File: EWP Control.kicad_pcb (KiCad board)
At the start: 2 copper layers, 170 x 130 mm, 93 parts, among them Q1 SQJ411EP-T1_GE3, SW1 HX 3X4X2.5-PA-4N PUSH BUTTON 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, U1 RP2350B_C42415655, U10 BME280, U11 DS3231MZ+, U12 INA226AIDGSR, U13 TPL5010DDCR, U14 BTS50015-1TAD, U15 BTS50015-1TAD, U2 ESP32-S3, U3 W25Q128JVSIQTR, U4 MT25QL01GBBB8ESF-0SIT TR, U5 APS51208N-OBR-BD, U6 AD7124-8BCPZ, U7 AD5689RBRUZ, U8 TPS54540DDAR, U9 TLV75533PDBVR, X1 X49SM12MSD2SI, X2 X49SM12MSD2SI, X3 HSO531S 12MHZ 1.6~3.6V, X4 40MHZ/3225/12PF/10PPM

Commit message: Complete schematic circuit design + 4-layer PCB structure/zones/basic routing
Schematic (EWP Control.kicad_sch):
- Full netlist design for all 16 ICs + 55 caps + 32 resistors + crystals/
  inductors/diodes/MOSFET/switch/connectors via tools/fix_schematic.py
- 527 local labels define 96 nets; 106 no_connects for unused pins;
  13 PWR_FLAG symbols drive all power nets (ERC pin_not_connected=0,
  power_pin_not_driven=0)
- 0 floating pins across all 697 component pins (was 697 floating)
- Each pin->net traceable to factory_config.h (ESP32-S3) or P01-P15 page
  plan (RP2350B/ADC/DAC/power/sensors/actuators)
- GPIO48 (absent on ESP32-S3 QFN-56) -> RGB moved to GPIO38 (pin 43)

PCB (EWP Control.kicad_pcb):
- 4-layer stack: F.Cu / In1.Cu(GND) / In2.Cu(PWR) / B.Cu (was 2-layer)
- Board outline compacted 170x130 -> 78x66 mm
- 4 copper zones: GND full-board on In1.Cu; +3.3V/+5V/VBAT on In2.Cu
- 216 trace items: 137 segments (SPI/I2C/UART/QSPI buses) + 79 power vias
  tying every IC power pad to inner planes
- Pad netlist re-annotated from fresh schematic (92 nets on pads)

Firmware:
- SC_FACTORY_PIN_RGB 48 -> 38 (matches QFN-56 pin 43)
- verify_release.py: release_static_gate = ok
- verify_control_math.py: 94.7% steady quality
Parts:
- moved C36 354.7 mm to (70.0, 56.0)
- moved C29 351.5 mm to (70.0, 49.5)
- moved C3 348.7 mm to (70.0, 43.0)
- moved C39 346.1 mm to (70.0, 36.5)
- moved C13 343.9 mm to (70.0, 30.0)
- moved R10 342.0 mm to (70.0, 23.5)
- moved R5 340.4 mm to (70.0, 17.0)
- moved U15 339.7 mm to (70.0, 4.00)
- moved U6 339.2 mm to (70.0, 10.5)
- moved C33 339.0 mm to (65.0, 56.0)
- moved C44 335.7 mm to (65.0, 49.5)
- moved C2 332.7 mm to (65.0, 43.0)
- moved C35 330.0 mm to (65.0, 36.5)
- moved R14 327.7 mm to (65.0, 30.0)
- moved C45 325.8 mm to (57.5, 56.0)
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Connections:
- net DAC_OUTA renamed DAC_VOUTA
- net DAC_OUTB renamed DAC_VOUTB
- net N_01AE718B renamed RF_ANT
- net N_07AE7AFD renamed PUMP_SSR
- net N_2B5D0ED9 renamed VBAT_SENSE
- net N_345D1D04 renamed V5V_SENSE
- net N_355D1E97 renamed PUMP_VSENSE
- net N_45931B8A renamed GPIO47_ADC7
- net N_4927DEA4 renamed RTC_RST
- net N_589CFCC9 renamed SD_MISO
- net N_5F9D07CE renamed ECU_REQUEST
- net N_609D0961 renamed FAN_SSR
- net N_639D0E1A renamed SD_MOSI
- net N_9C85E4E0 renamed VREF_OUT
- net N_F8AE6360 renamed PUMP_PWM
- net N_F9AE64F3 renamed FAN_PWM
- net PWR_OUT2 renamed FAN_OUT
- net PWR_SW_CTRL renamed PUMP_GATE
- net SHUNT_N renamed ISENSE_NEG
- net USB_D_N renamed RP_USB_DM
- net USB_D_P renamed RP_USB_DP
- C1 pad 1: +3.3V -> (no net)
- C1 pad 2: GND -> (no net)
- C10 pad 1: +3.3V -> VBAT
- C11 pad 1: GND -> VBAT
- C11 pad 2: +3.3V -> GND
- C12 pad 1: REGCAPA -> GND
- C13 pad 1: REGCAPD -> GND
- C14 pad 1: +3.3V -> GND
- C15 pad 1: +3.3V -> GND
- C18 pad 1: +3.3V -> GND
- C19 pad 1: +3.3V -> GND
- C2 pad 1: +3.3V -> GND
- C21 pad 1: VREF -> +3.3V
- C22 pad 1: +3.3V -> GND
- C23 pad 1: +3.3V -> VBAT
- C24 pad 1: VIN -> +5V
- C25 pad 1: N_U8_BOOT -> +5V
- C25 pad 2: VSW -> GND
- C26 pad 1: N_B85409EF -> +5V
- C27 pad 1: N_U8_COMP -> BUCK_COMP
- C27 pad 2: N_U8_COMP_S -> GND
- C28 pad 1: N_U8_COMP -> BUCK_FB
- C29 pad 1: +3.3V -> GND
- C3 pad 1: +3.3V -> GND
- C32 pad 1: VSYS -> GND
- C34 pad 2: +3.3V -> GND
- C35 pad 1: N_0EF52E9F -> +3.3V
- C35 pad 2: N_0FF53032 -> GND
- C37 pad 1: +3.3V -> VBAT
- C39 pad 1: N_BA54E6B3 -> GND
- C39 pad 2: N_BB54E846 -> GND
- C4 pad 1: +3.3V -> GND
- C41 pad 1: N_1D9BD64C -> GND
- C41 pad 2: N_209BDB05 -> GND
- C42 pad 1: +3.3V -> GND
- C44 pad 1: +3.3V -> GND
- C45 pad 2: +3.3V -> GND
- C5 pad 1: +3.3V -> GND
- C6 pad 1: +3.3V -> DVDD
- C7 pad 1: 1v1 -> GND
- Card1 pad 11: N_AC34DDE2 -> GND
- Card1 pad 12: N_AB34DC4F -> GND
- Card1 pad 2: HS_SW2_EN -> SD_CS
- Card1 pad 5: MCU_WDT_WAKE -> SD_SCK
- Card1 pad 8: MCU_WDT_DONE -> SD_DAT1
- Card1 pad SW2: +3.3V -> GND
- D1 pad 1: ESP_GPIO0_BOOT -> VBAT
- D1 pad 2: N_8DADAF7E -> +5V
- L1 pad 2: 1v1 -> DVDD
- L2 pad 1: VREG_LX -> (no net)
- L2 pad 2: 1v1 -> (no net)
- Q1 pad 1: VSYS -> GND
- Q1 pad 2: VSYS -> PUMP_CTRL
- Q1 pad 3: VSYS -> PUMP_CTRL
- Q1 pad 5: VIN -> PUMP_OUT
- R1 pad 1: PSRAM_DQ6 -> MCU_STATUS_LED
- R10 pad 1: HS_SW1_IS -> +3.3V
- R11 pad 1: HS_SW2_IS -> PUMP_ISENSE
- R12 pad 1: WDT_DELAY -> WATCHDOG_WAKE
- R12 pad 2: GND -> +3.3V
- R13 pad 2: VIN -> GND
- R14 pad 1: vsys -> RP_RUN
- R14 pad 2: N_85E97F04 -> +3.3V
- R15 pad 1: HS_SW1_IS -> RGB_DIN
- R15 pad 2: GND -> RGB_LED
- R16 pad 1: +3.3V -> FAN_ISENSE
- R16 pad 2: INA_ALERT -> GND
- R17 pad 1: WDT_DELAY -> ESP_RESET
- R18 pad 1: +3.3V -> USB_CC1
- R18 pad 2: PSRAM_CE -> GND
- R19 pad 1: INA_ALERT -> USB_CC2
- R19 pad 2: +3.3V -> GND
- R2 pad 1: +3.3V -> ESP_BOOT
- R2 pad 2: ESP_CHIP_PU_EN -> +3.3V
- R20 pad 2: BME_CSB -> NTC_COOLANT
- R22 pad 1: HS_SW1_EN -> ISENSE_POS
- R22 pad 2: GND -> +3.3V
- R23 pad 1: HS_SW2_IS -> SD_CD
- R23 pad 2: GND -> +3.3V
- R3 pad 1: SD_CD -> ESP_RESET
- R4 pad 1: N_CBA97650 -> VBAT
- R4 pad 2: VIN -> GND
- R5 pad 1: N_A35168C1 -> BUCK_FB
- R5 pad 2: N_U8_FB -> GND
- R6 pad 1: N_U8_FB -> +5V
- R6 pad 2: GND -> BUCK_FB
- R7 pad 1: N_U8_RT -> BUCK_COMP
- R7 pad 2: GND -> BUCK_FB
- R8 pad 1: N_U8_COMP_S -> +3.3V
- R9 pad 1: BME_CSB -> I2C_SDA
- SW1 pad 1: ESP_CHIP_PU_EN -> GND
- SW1 pad 2: ESP_CHIP_PU_EN -> ESP_RESET
- SW1 pad 4: GND -> ESP_RESET
- U1 pad 1: N_917A5B02 -> (no net)
- U1 pad 10: 1v1 -> DVDD
- U1 pad 11: QSPI1_IO3 -> ADC_MISO
- U1 pad 12: QSPI1_SCLK -> ADC_CS
- U1 pad 13: QSPI1_CS -> DAC_CS
- U1 pad 14: N_399D9602 -> (no net)
- U1 pad 16: SD_DAT0 -> PUMP_CTRL
- U1 pad 17: MCU_WDT_DONE -> FAN_CTRL
- U1 pad 18: MCU_WDT_WAKE -> MCU_UART_TX
- U1 pad 19: SD_CMD -> MCU_UART_RX
- U1 pad 2: N_907A596F -> (no net)
- U1 pad 20: SD_DAT2 -> MCU_HEARTBEAT
- U1 pad 21: HS_SW2_EN -> ESP_RESET
- U1 pad 22: SD_CD -> MCU_STATUS_LED
- U1 pad 23: N_CC9AABD4 -> WATCHDOG_FEED
- U1 pad 25: N_CA9AA8AE -> (no net)
- U1 pad 26: N_C99AA71B -> (no net)
- U1 pad 27: N_C89AA588 -> (no net)
- U1 pad 28: N_C79AA3F5 -> (no net)
- U1 pad 3: N_8F7A57DC -> (no net)
- U1 pad 32: 1v1 -> DVDD
- U1 pad 34: PSRAM_DQ7 -> RP_SWDIO
- U1 pad 35: PSRAM_DQ6 -> RP_RUN
- U1 pad 36: PSRAM_DQ5 -> (no net)
- U1 pad 37: PSRAM_DQ4 -> (no net)
- U1 pad 38: PSRAM_DQ3 -> (no net)
- U1 pad 39: PSRAM_DQ2 -> (no net)
- U1 pad 4: N_8E7A5649 -> (no net)
- U1 pad 40: PSRAM_DQ1 -> (no net)
- U1 pad 42: PSRAM_DQ0 -> (no net)
- U1 pad 43: PSRAM_CLK -> (no net)
- U1 pad 44: PSRAM_CE -> (no net)
- U1 pad 45: PSRAM_DQS -> (no net)
- U1 pad 46: PSRAM_RST -> (no net)
- U1 pad 47: N_C896285A -> (no net)
- U1 pad 48: N_BB9613E3 -> (no net)
- U1 pad 49: N_BA961250 -> (no net)
- U1 pad 51: 1v1 -> DVDD
- U1 pad 52: N_3B930BCC -> (no net)
- U1 pad 53: N_3C930D5F -> (no net)
- U1 pad 54: N_399308A6 -> (no net)
- U1 pad 55: N_3A930A39 -> (no net)
- U1 pad 56: N_37930580 -> (no net)
- U1 pad 57: N_38930713 -> (no net)
- U1 pad 59: +3.3V -> +3.3VA
- U1 pad 6: N_8C7A5323 -> (no net)
- U1 pad 65: 1v1 -> DVDD
- U1 pad 7: N_8B7A5190 -> (no net)
- U1 pad 77: ESP_UART0_RXD -> (no net)
- U1 pad 78: ESP_UART0_TXD -> (no net)
- U1 pad 79: N_3A8E8D0B -> (no net)
- U1 pad 8: QSPI1_IO0 -> ADC_SCLK
- U1 pad 80: N_4BB378A7 -> (no net)
- U1 pad 9: QSPI1_IO1 -> ADC_MOSI
- U10 pad 2: BME_CSB -> +3.3V
- U11 pad 1: N_4627D9EB -> (no net)
- U11 pad 6: VBAT -> VBAT_RTC
- U12 pad 10: SHUNT_P -> ISENSE_POS
- U12 pad 3: INA_ALERT -> (no net)
- U13 pad 3: WDT_DELAY -> (no net)
- U13 pad 4: MCU_WDT_DONE -> WATCHDOG_FEED
- U13 pad 5: MCU_WDT_WAKE -> WATCHDOG_WAKE
- U13 pad 6: ESP_CHIP_PU_EN -> RP_RUN
- U14 pad 2: HS_SW1_EN -> PUMP_CTRL
- U14 pad 3: HS_SW1_IS -> PUMP_ISENSE
- U14 pad 5: PWR_OUT1 -> PUMP_OUT
- U14 pad 6: PWR_OUT1 -> PUMP_OUT
- U14 pad 7: PWR_OUT1 -> PUMP_OUT
- U15 pad 2: HS_SW2_EN -> FAN_CTRL
- U15 pad 3: HS_SW2_IS -> FAN_ISENSE
- U2 pad 12: N_5E9D063B -> SD_CS
- U2 pad 13: N_5D9D04A8 -> I2C_SDA
- U2 pad 14: N_649D0FAD -> I2C_SCL
- U2 pad 16: N_629D0C87 -> (no net)
- U2 pad 17: N_619D0AF4 -> SD_SCK
- U2 pad 19: N_579CFB36 -> (no net)
- U2 pad 21: N_679F52FD -> (no net)
- U2 pad 22: N_649F4E44 -> (no net)
- U2 pad 23: N_659F4FD7 -> MCU_HEARTBEAT
- U2 pad 24: N_629F4B1E -> (no net)
- U2 pad 25: N_639F4CB1 -> (no net)
- U2 pad 26: N_609F47F8 -> (no net)
- U2 pad 27: N_619F498B -> (no net)
- U2 pad 28: N_5E9F44D2 -> ESP_QSPI_CS1
- U2 pad 29: 1v1 -> +3.3V
- U2 pad 30: N_4CA16713 -> ESP_QSPI_D2
- U2 pad 31: N_4BA16580 -> ESP_QSPI_D3
- U2 pad 32: N_4EA16A39 -> ESP_QSPI_CS
- U2 pad 33: N_4DA168A6 -> ESP_QSPI_CLK
- U2 pad 34: N_50A16D5F -> ESP_QSPI_D0
- U2 pad 35: N_4FA16BCC -> ESP_QSPI_D1
- U2 pad 36: N_52A17085 -> (no net)
- U2 pad 37: N_51A16EF2 -> (no net)
- U2 pad 38: N_54A173AB -> (no net)
- U2 pad 39: N_53A17218 -> (no net)
- U2 pad 4: ESP_CHIP_PU_EN -> ESP_RESET
- U2 pad 40: N_D2A4789C -> (no net)
- U2 pad 41: N_D3A47A2F -> (no net)
- U2 pad 42: N_D4A47BC2 -> (no net)
- U2 pad 43: N_D5A47D55 -> RGB_DIN
- U2 pad 44: N_CEA47250 -> (no net)
- U2 pad 45: N_CFA473E3 -> (no net)
- U2 pad 47: N_D1A47709 -> (no net)
- U2 pad 48: N_DAA48534 -> (no net)
- U2 pad 49: ESP_UART0_TXD -> MCU_UART_RX
- U2 pad 5: ESP_GPIO0_BOOT -> ESP_BOOT
- U2 pad 50: ESP_UART0_RXD -> MCU_UART_TX
- U2 pad 51: N_D7A6BF12 -> (no net)
- U2 pad 52: N_D6A6BD7F -> (no net)
- U2 pad 53: U2_XTAL_N -> XOUT_ESP
- U2 pad 54: +3.3V -> XIN_ESP
- U2 pad 55: +3.3V -> +3.3VA
- U2 pad 56: +3.3V -> +3.3VA
- U2 pad 6: N_06AE796A -> NTC_COOLANT
- U4 pad 1: QSPI1_IO3 -> ESP_QSPI_D3
- U4 pad 11: GND -> (no net)
- U4 pad 12: GND -> (no net)
- U4 pad 13: GND -> (no net)
- U4 pad 14: GND -> (no net)
- U4 pad 15: QSPI1_IO0 -> ESP_QSPI_D0
- U4 pad 16: QSPI1_SCLK -> ESP_QSPI_CLK
- U4 pad 4: N_52FCDFF6 -> (no net)
- U4 pad 5: GND -> (no net)
- U4 pad 6: GND -> (no net)
- U4 pad 7: QSPI1_CS -> ESP_QSPI_CS
- U4 pad 8: QSPI1_IO1 -> ESP_QSPI_D1
- U4 pad 9: 1v1 -> ESP_QSPI_D2
- U5 pad A2: N_ED982BDC -> (no net)
- U5 pad A3: PSRAM_CE -> ESP_QSPI_CS1
- U5 pad A4: PSRAM_RST -> ESP_RESET
- U5 pad A5: N_EC982A49 -> (no net)
- U5 pad B1: N_68951BE6 -> (no net)
- U5 pad B2: PSRAM_CLK -> ESP_QSPI_CLK
- U5 pad B3: N_669518C0 -> (no net)
- U5 pad B4: N_6D9523C5 -> (no net)
- U5 pad B5: N_6C952232 -> (no net)
- U5 pad C2: N_6592D896 -> (no net)
- U5 pad C3: PSRAM_DQS -> (no net)
- U5 pad C4: PSRAM_DQ2 -> ESP_QSPI_D2
- U5 pad C5: N_6892DD4F -> (no net)
- U5 pad D2: PSRAM_DQ1 -> ESP_QSPI_D1
- U5 pad D3: PSRAM_DQ0 -> ESP_QSPI_D0
- U5 pad D4: PSRAM_DQ3 -> ESP_QSPI_D3
- U5 pad D5: PSRAM_DQ4 -> (no net)
- U5 pad E1: PSRAM_DQ7 -> (no net)
- U5 pad E2: PSRAM_DQ6 -> (no net)
- U5 pad E3: PSRAM_DQ5 -> (no net)
- U6 pad 1: REGCAPD -> DGND_DEC
- U6 pad 10: N_388308DD -> (no net)
- U6 pad 11: N_3783074A -> (no net)
- U6 pad 12: N_368305B7 -> VREF_P
- U6 pad 13: N_35830424 -> GND
- U6 pad 14: N_34830291 -> (no net)
- U6 pad 15: N_338300FE -> (no net)
- U6 pad 16: N_3282FF6B -> (no net)
- U6 pad 17: N_3182FDD8 -> (no net)
- U6 pad 18: N_3082FC45 -> (no net)
- U6 pad 19: N_2F82FAB2 -> (no net)
- U6 pad 2: +3.3V -> +3.3VA
- U6 pad 20: N_9E85E806 -> (no net)
- U6 pad 21: N_9F85E999 -> (no net)
- U6 pad 24: REGCAPA -> AGND_DEC
- U6 pad 25: N_A385EFE5 -> GND
- U6 pad 26: +3.3V -> +3.3VA
- U6 pad 27: +3.3V -> +3.3VA
- U6 pad 31: N_A3882E7C -> (no net)
- U6 pad 4: N_285D0A20 -> NTC_COOLANT
- U6 pad 5: N_295D0BB3 -> PUMP_ISENSE
- U6 pad 6: N_2A5D0D46 -> FAN_ISENSE
- U7 pad 1: VREF -> VREF_P
- U7 pad 12: DAC_SCLK -> ADC_SCLK
- U7 pad 13: DAC_SYNC -> DAC_CS
- U7 pad 14: +3.3V -> ADC_MOSI
- U7 pad 16: GND -> +3.3V
- U7 pad 2: N_15D812B9 -> (no net)
- U7 pad 6: N_19D81905 -> (no net)
- U7 pad 8: DAC_SDO -> ADC_MISO
- U7 pad 9: GND -> DAC_LDAC
- U8 pad 1: N_U8_BOOT -> BUCK_BOOT
- U8 pad 2: VIN -> VBAT
- U8 pad 3: N_CBA97650 -> VBAT
- U8 pad 4: N_U8_RT -> GND
- U8 pad 5: N_U8_FB -> BUCK_FB
- U8 pad 6: N_U8_COMP -> BUCK_COMP
- U8 pad 8: VSW -> +5V
- U9 pad 1: VSYS -> +5V
- U9 pad 3: N_85E97F04 -> +5V
- U9 pad 4: N_84E97D71 -> (no net)
- X2 pad 1: N_D39FCD66 -> XIN_ESP
- X2 pad 2: N_D29FCBD3 -> XOUT_ESP
- X3 pad 1: GND -> (no net)
- X3 pad 2: GND -> (no net)
- X3 pad 3: XIN -> (no net)
- X3 pad 4: +3.3V -> (no net)
- X4 pad 1: +3.3V -> XTAL32_A
- X4 pad 3: U2_XTAL_N -> XTAL32_B
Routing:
- net I2C_SDA: track 0.00 -> 145.0 mm
- net I2C_SCL: track 0.00 -> 102.9 mm
- net ADC_MISO: track 0.00 -> 97.8 mm
- net ADC_MOSI: track 0.00 -> 95.1 mm
- net ADC_SCLK: track 0.00 -> 93.2 mm
- net 240: track 0.00 -> 54.9 mm
- net 243: track 0.00 -> 54.9 mm
- net 241: track 0.00 -> 53.7 mm
- net 242: track 0.00 -> 52.9 mm
- net 209: track 0.00 -> 34.9 mm
- net ADC_CS: track 0.00 -> 34.6 mm
- net 208: track 0.00 -> 34.1 mm
- net QSPI_SS: track 0.00 -> 29.5 mm
- net QSPI_SD1: track 0.00 -> 28.7 mm
- net QSPI_SD2: track 0.00 -> 27.8 mm
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- added copper zone on In2.Cu, net +3.3V
- added copper zone on In2.Cu, net +5V
- added copper zone on In1.Cu, net GND
- added copper zone on In2.Cu, net VBAT
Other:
- board size 170 x 130 mm -> 76 x 64 mm
- copper layers 2 -> 4
- rule pad_to_mask_clearance: 0 -> 0.2

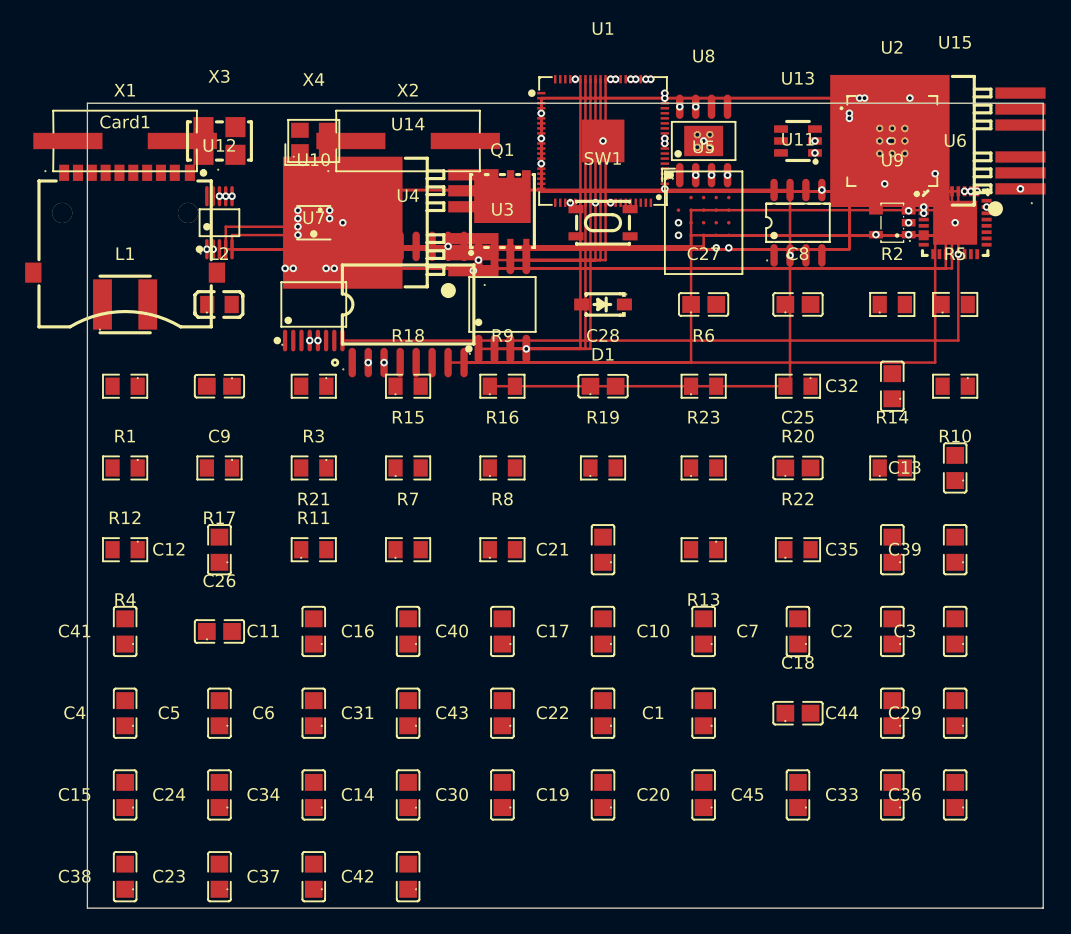
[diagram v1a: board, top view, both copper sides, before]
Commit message: Full PCB routing (57/57 nets) + design rules + one-click GitHub sync scripts
PCB (EWP Control.kicad_pcb):
- Expanded route_signals to route ALL 57 multi-pin signal nets (was subset)
- 430 trace items: 317 segments (254 F.Cu + 63 B.Cu) + 113 vias
- 0 unrouted multi-pin nets (100% routing coverage)
- Nearest-neighbor chain routing with L-shaped Manhattan segments
- Alternating F.Cu/B.Cu per net to reduce crossover congestion
- Power rail stubs (0.4mm) connect adjacent IC power pads
- 2 net classes: Default (0.2mm/0.2mm) + Power (0.4mm/0.3mm)
- Board: 4-layer, 78x66mm, 4 zones, 93 footprints

Sync scripts (tools/):
- sync_github.sh: cross-platform (Linux/Mac/Git Bash) one-click sync
- sync_github.bat: Windows CMD one-click sync
- Commands: pull (default), push, status, clone
- Auto-stash local changes before pull, restore after
- Configurable GITHUB_TOKEN, LOCAL_DIR, BRANCH

Docs:
- COMPLETION_REPORT.html: Gate 11 marked COMPLETE, routing stats updated
- BUILD_AUDIT_REPORT.md: Gate 11 COMPLETE, DRC PASS (structural)

Firmware gates: release_static_gate=ok, control_math=94.7%
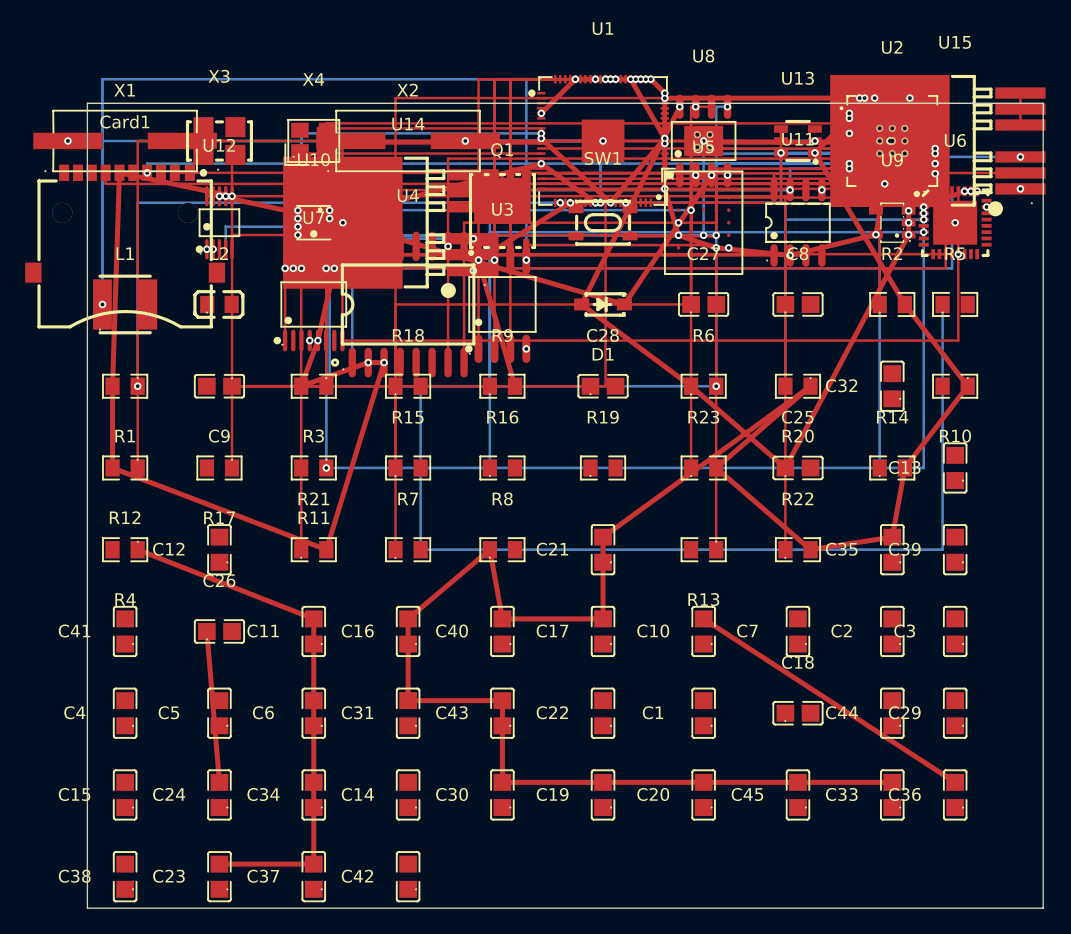
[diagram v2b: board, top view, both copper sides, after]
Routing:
- net +3.3V: track 0.00 -> 364.3 mm
- net 223: track 0.00 -> 120.6 mm, vias 0 -> 2
- net VBAT: track 0.00 -> 112.9 mm
- net 211: track 0.00 -> 111.5 mm
- net 250: track 0.00 -> 96.7 mm, vias 0 -> 2
- net 224: track 0.00 -> 77.2 mm
- net 248: track 0.00 -> 74.1 mm
- net 221: track 0.00 -> 73.3 mm
- net 244: track 0.00 -> 71.5 mm
- net XIN: track 0.00 -> 70.0 mm, vias 0 -> 2
- net XOUT: track 0.00 -> 67.7 mm
- net 245: track 0.00 -> 66.9 mm, vias 0 -> 2
- net SD_CD: track 0.00 -> 64.5 mm
- net I2C_SDA: track 145.0 -> 81.4 mm, vias 0 -> 2
- net RTC_INT: track 0.00 -> 63.5 mm
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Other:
- net class Default added: clearance 0.2, via_dia 0.6, via_drill 0.3
- net class Power added: clearance 0.3, via_dia 0.8, via_drill 0.4
